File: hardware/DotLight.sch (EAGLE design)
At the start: 21 parts, among them Q1 BSH103, Q2 BSH103

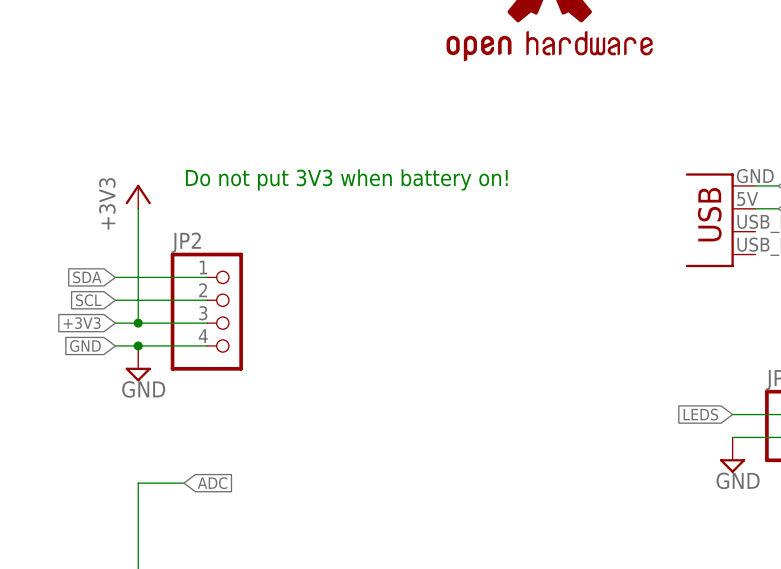
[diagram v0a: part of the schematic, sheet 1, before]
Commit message: Mirror parts for space for PIR
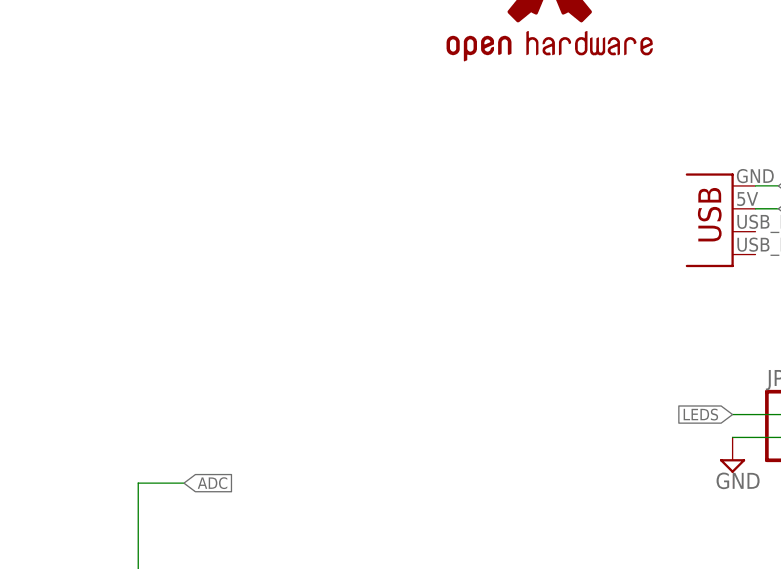
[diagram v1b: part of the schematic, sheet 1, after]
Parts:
- removed JP2: (no value), pinhead:PINHD-1X4
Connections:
- removed net +3V3: JP2.3
- removed net SCL: JP2.2
- removed net SDA: JP2.1
- net GND: no longer JP2.4
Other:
- note removed: "Do not put 3V3 when battery on!"
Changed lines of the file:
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@@
 </classes>
 <parts>
-<part name="+3V6" library="supply1" deviceset="+3V3" device=""/>
-<part name="JP2" library="pinhead" deviceset="PINHD-1X4" device=""/>
 <part name="SUPPLY1" library="supply2" deviceset="GND" device=""/>
-<part name="SUPPLY18" library="supply2" deviceset="GND" device=""/>
 <part name="JP1" library="pinhead" deviceset="PINHD-1X10" device=""/>
 <part name="JP8" library="pinhead" deviceset="PINHD-1X2" device=""/>
@@
 <sheet>
 <plain>
-<text x="71.12" y="195.58" size="1.778" layer="91">Do not put 3V3 when battery on!</text>
 <text x="114.3" y="124.46" size="1.27" layer="91">Emit</text>
 <text x="139.7" y="124.46" size="1.27" layer="91">Sense</text>
 </plain>
 <instances>
-<instance part="+3V6" gate="G$1" x="66.04" y="195.58"/>
-<instance part="JP2" gate="A" x="76.2" y="180.34"/>
 <instance part="SUPPLY1" gate="GND" x="93.98" y="134.62" rot="R90"/>
-<instance part="SUPPLY18" gate="GND" x="66.04" y="175.26"/>
 <instance part="JP1" gate="A" x="78.74" y="134.62"/>
 <instance part="JP8" gate="G$1" x="142.24" y="167.64"/>
@@
 </segment>
 <segment>
-<pinref part="JP2" gate="A" pin="4"/>
-<wire x1="73.66" y1="177.8" x2="66.04" y2="177.8" width="0.1524" layer="91"/>
-<pinref part="SUPPLY18" gate="GND" pin="GND"/>
-<wire x1="66.04" y1="177.8" x2="63.5" y2="177.8" width="0.1524" layer="91"/>
-<junction x="66.04" y="177.8"/>
-<label x="63.5" y="177.8" size="1.27" layer="95" rot="R180" xref="yes"/>
-</segment>
-<segment>
 <pinref part="JP8" gate="G$1" pin="2"/>
 <wire x1="139.7" y1="167.64" x2="132.08" y2="167.64" width="0.1524" layer="91"/>
@@
 </segment>
 </net>
-<net name="SDA" class="0">
-<segment>
-<pinref part="JP2" gate="A" pin="1"/>
-<wire x1="73.66" y1="185.42" x2="63.5" y2="185.42" width="0.1524" layer="91"/>
-<label x="63.5" y="185.42" size="1.27" layer="95" rot="R180" xref="yes"/>
-</segment>
-</net>
 <net name="RST" class="0">
 <segment>
@@
 <pinref part="JP1" gate="A" pin="7"/>
 <wire x1="60.96" y1="129.54" x2="76.2" y2="129.54" width="0.1524" layer="91"/>
-</segment>
-</net>
-<net name="+3V3" class="0">
-<segment>
-<pinref part="JP2" gate="A" pin="3"/>
-<wire x1="73.66" y1="180.34" x2="66.04" y2="180.34" width="0.1524" layer="91"/>
-<pinref part="+3V6" gate="G$1" pin="+3V3"/>
-<wire x1="66.04" y1="180.34" x2="63.5" y2="180.34" width="0.1524" layer="91"/>
-<wire x1="66.04" y1="193.04" x2="66.04" y2="180.34" width="0.1524" layer="91"/>
-<junction x="66.04" y="180.34"/>
-<label x="63.5" y="180.34" size="1.27" layer="95" rot="R180" xref="yes"/>
 </segment>
 </net>
@@
 </segment>
 </net>
-<net name="SCL" class="0">
-<segment>
-<pinref part="JP2" gate="A" pin="2"/>
-<wire x1="73.66" y1="182.88" x2="63.5" y2="182.88" width="0.1524" layer="91"/>
-<label x="63.5" y="182.88" size="1.27" layer="95" rot="R180" xref="yes"/>
-</segment>
-</net>

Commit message: Adjust solderjumpers
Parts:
- removed SJ1: SOLDERJUMPERTRACE, SparkFun-Retired:SOLDERJUMPERTRACE
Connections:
- net N$4 renamed GO
- net LEDS: no longer SJ1.1
- net VIN_PIN: no longer SJ1.2
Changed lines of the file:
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@@
 <part name="R6" library="resistor" deviceset="R-EU_" device="R1206" value="1MΩ"/>
 <part name="SJ2" library="SparkFun-Retired" deviceset="SOLDERJUMPER" device="NO"/>
-<part name="SJ1" library="SparkFun-Retired" deviceset="SOLDERJUMPER" device="TRACE"/>
 </parts>
 <sheets>
@@
 <instance part="R6" gate="G$1" x="129.54" y="121.92"/>
 <instance part="SJ2" gate="1" x="193.04" y="200.66" rot="MR270"/>
-<instance part="SJ1" gate="1" x="172.72" y="203.2" rot="R90"/>
 </instances>
 <busses>
@@
 <segment>
 <pinref part="Q1" gate="G$1" pin="D"/>
-<wire x1="182.88" y1="205.74" x2="182.88" y2="208.28" width="0.1524" layer="91"/>
 <label x="182.88" y="210.82" size="1.27" layer="95" xref="yes"/>
 <pinref part="SJ2" gate="1" pin="1"/>
-<wire x1="182.88" y1="208.28" x2="182.88" y2="210.82" width="0.1524" layer="91"/>
+<wire x1="182.88" y1="205.74" x2="182.88" y2="210.82" width="0.1524" layer="91"/>
 <wire x1="182.88" y1="205.74" x2="193.04" y2="205.74" width="0.1524" layer="91"/>
 <junction x="182.88" y="205.74"/>
-<pinref part="SJ1" gate="1" pin="2"/>
-<wire x1="172.72" y1="208.28" x2="182.88" y2="208.28" width="0.1524" layer="91"/>
-<junction x="182.88" y="208.28"/>
 </segment>
 </net>
@@
 <label x="167.64" y="198.12" size="1.27" layer="95" rot="R180" xref="yes"/>
 <pinref part="Q1" gate="G$1" pin="G"/>
-<wire x1="167.64" y1="198.12" x2="172.72" y2="198.12" width="0.1524" layer="91"/>
-<pinref part="SJ1" gate="1" pin="1"/>
-<wire x1="172.72" y1="198.12" x2="177.8" y2="198.12" width="0.1524" layer="91"/>
-<junction x="172.72" y="198.12"/>
+<wire x1="167.64" y1="198.12" x2="177.8" y2="198.12" width="0.1524" layer="91"/>
 </segment>
 <segment>
@@
 </segment>
 </net>
-<net name="N$4" class="0">
+<net name="GO" class="0">
 <segment>
 <pinref part="Q1" gate="G$1" pin="S"/>
